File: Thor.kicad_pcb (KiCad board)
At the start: 4 copper layers, 300 x 200 mm, 41 parts, among them J1 Conn_02x32_Counter_Clockwise, J2 Conn_02x32_Counter_Clockwise, J3 Conn_01x01, J4 Conn_01x01, Q1 PHP79NQ08LT, Q2 PHP79NQ08LT, Q3 PHP79NQ08LT, Q4 PHP79NQ08LT, Q5 PHP79NQ08LT, Q6 PHP79NQ08LT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

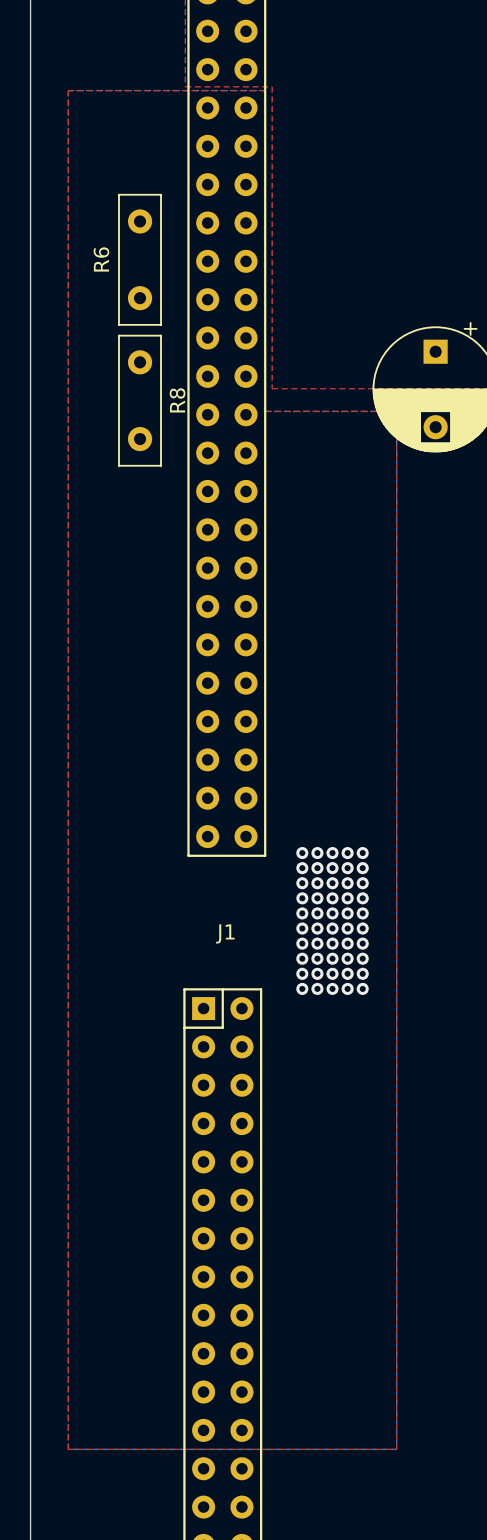
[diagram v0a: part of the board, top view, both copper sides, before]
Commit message: Revert "most recent version"
This reverts commit 98a59f1a5a33474df10b14d2ac29c781506322cc.
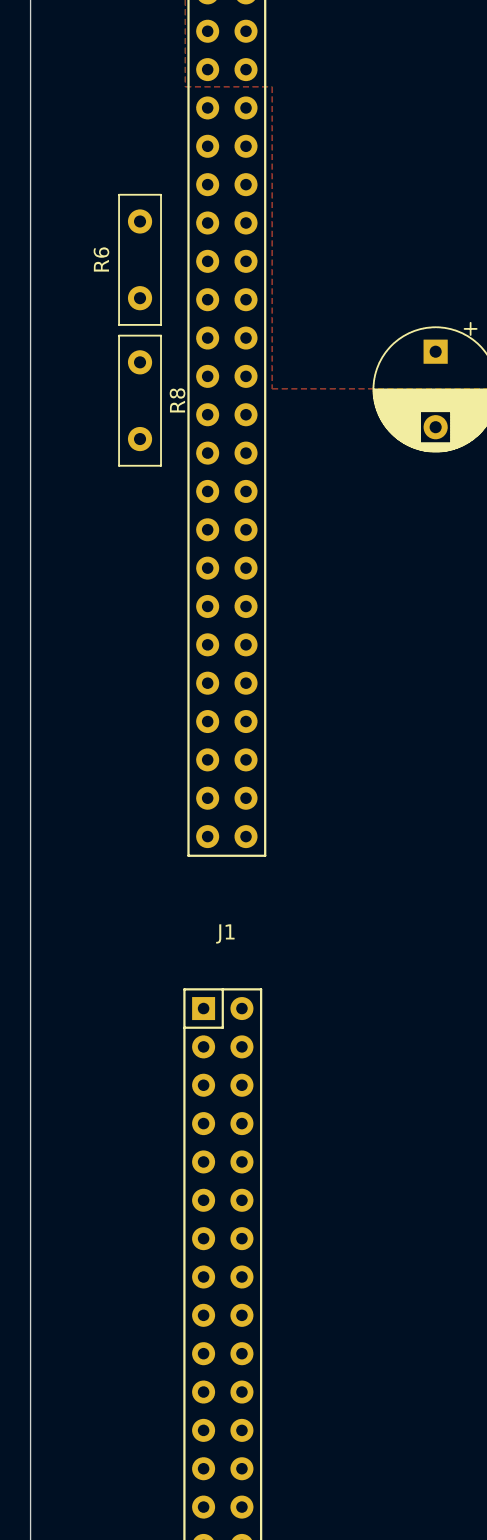
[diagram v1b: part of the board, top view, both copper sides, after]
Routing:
- net /12V_IN: vias 50 -> 0
- removed copper zone on B.Cu, net /12V_IN
- removed copper zone on F.Cu, net /12V_IN
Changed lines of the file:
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@@
     (thickness 1.6)
     (drawings 4)
-    (tracks 255)
+    (tracks 205)
     (zones 0)
     (modules 41)
@@
   (segment (start 157.9325 88.4) (end 158.48 88.9475) (width 0.25) (layer F.Cu) (net 42))
   (segment (start 156.4875 88.4) (end 157.9325 88.4) (width 0.25) (layer F.Cu) (net 42))
-  (via (at 28 100) (size 0.8) (drill 0.4) (layers F.Cu B.Cu) (net 44))
-  (via (at 29 100) (size 0.8) (drill 0.4) (layers F.Cu B.Cu) (net 44))
-  (via (at 30 100) (size 0.8) (drill 0.4) (layers F.Cu B.Cu) (net 44))
-  (via (at 31 100) (size 0.8) (drill 0.4) (layers F.Cu B.Cu) (net 44))
-  (via (at 32 100) (size 0.8) (drill 0.4) (layers F.Cu B.Cu) (net 44))
-  (via (at 28 101) (size 0.8) (drill 0.4) (layers F.Cu B.Cu) (net 44))
-  (via (at 29 101) (size 0.8) (drill 0.4) (layers F.Cu B.Cu) (net 44))
-  (via (at 30 101) (size 0.8) (drill 0.4) (layers F.Cu B.Cu) (net 44))
-  (via (at 31 101) (size 0.8) (drill 0.4) (layers F.Cu B.Cu) (net 44))
-  (via (at 32 101) (size 0.8) (drill 0.4) (layers F.Cu B.Cu) (net 44))
-  (via (at 28 102) (size 0.8) (drill 0.4) (layers F.Cu B.Cu) (net 44))
-  (via (at 29 102) (size 0.8) (drill 0.4) (layers F.Cu B.Cu) (net 44))
-  (via (at 30 102) (size 0.8) (drill 0.4) (layers F.Cu B.Cu) (net 44))
-  (via (at 31 102) (size 0.8) (drill 0.4) (layers F.Cu B.Cu) (net 44))
-  (via (at 32 102) (size 0.8) (drill 0.4) (layers F.Cu B.Cu) (net 44))
-  (via (at 28 103) (size 0.8) (drill 0.4) (layers F.Cu B.Cu) (net 44))
-  (via (at 29 103) (size 0.8) (drill 0.4) (layers F.Cu B.Cu) (net 44))
-  (via (at 30 103) (size 0.8) (drill 0.4) (layers F.Cu B.Cu) (net 44))
-  (via (at 31 103) (size 0.8) (drill 0.4) (layers F.Cu B.Cu) (net 44))
-  (via (at 32 103) (size 0.8) (drill 0.4) (layers F.Cu B.Cu) (net 44))
-  (via (at 28 104) (size 0.8) (drill 0.4) (layers F.Cu B.Cu) (net 44))
-  (via (at 29 104) (size 0.8) (drill 0.4) (layers F.Cu B.Cu) (net 44))
-  (via (at 30 104) (size 0.8) (drill 0.4) (layers F.Cu B.Cu) (net 44))
-  (via (at 31 104) (size 0.8) (drill 0.4) (layers F.Cu B.Cu) (net 44))
-  (via (at 32 104) (size 0.8) (drill 0.4) (layers F.Cu B.Cu) (net 44))
-  (via (at 28 105) (size 0.8) (drill 0.4) (layers F.Cu B.Cu) (net 44))
-  (via (at 29 105) (size 0.8) (drill 0.4) (layers F.Cu B.Cu) (net 44))
-  (via (at 30 105) (size 0.8) (drill 0.4) (layers F.Cu B.Cu) (net 44))
-  (via (at 31 105) (size 0.8) (drill 0.4) (layers F.Cu B.Cu) (net 44))
-  (via (at 32 105) (size 0.8) (drill 0.4) (layers F.Cu B.Cu) (net 44))
-  (via (at 28 106) (size 0.8) (drill 0.4) (layers F.Cu B.Cu) (net 44))
-  (via (at 29 106) (size 0.8) (drill 0.4) (layers F.Cu B.Cu) (net 44))
-  (via (at 30 106) (size 0.8) (drill 0.4) (layers F.Cu B.Cu) (net 44))
-  (via (at 31 106) (size 0.8) (drill 0.4) (layers F.Cu B.Cu) (net 44))
-  (via (at 32 106) (size 0.8) (drill 0.4) (layers F.Cu B.Cu) (net 44))
-  (via (at 28 107) (size 0.8) (drill 0.4) (layers F.Cu B.Cu) (net 44))
-  (via (at 29 107) (size 0.8) (drill 0.4) (layers F.Cu B.Cu) (net 44))
-  (via (at 30 107) (size 0.8) (drill 0.4) (layers F.Cu B.Cu) (net 44))
-  (via (at 31 107) (size 0.8) (drill 0.4) (layers F.Cu B.Cu) (net 44))
-  (via (at 32 107) (size 0.8) (drill 0.4) (layers F.Cu B.Cu) (net 44))
-  (via (at 28 108) (size 0.8) (drill 0.4) (layers F.Cu B.Cu) (net 44))
-  (via (at 29 108) (size 0.8) (drill 0.4) (layers F.Cu B.Cu) (net 44))
-  (via (at 30 108) (size 0.8) (drill 0.4) (layers F.Cu B.Cu) (net 44))
-  (via (at 31 108) (size 0.8) (drill 0.4) (layers F.Cu B.Cu) (net 44))
-  (via (at 32 108) (size 0.8) (drill 0.4) (layers F.Cu B.Cu) (net 44))
-  (via (at 28 109) (size 0.8) (drill 0.4) (layers F.Cu B.Cu) (net 44))
-  (via (at 29 109) (size 0.8) (drill 0.4) (layers F.Cu B.Cu) (net 44))
-  (via (at 30 109) (size 0.8) (drill 0.4) (layers F.Cu B.Cu) (net 44))
-  (via (at 31 109) (size 0.8) (drill 0.4) (layers F.Cu B.Cu) (net 44))
-  (via (at 32 109) (size 0.8) (drill 0.4) (layers F.Cu B.Cu) (net 44))
   (zone (net 32) (net_name /SW) (layer F.Cu) (hatch edge 0.508)
     (connect_pads yes (clearance 0.508))
@@
       )
     )
-  )
-  (zone (net 44) (net_name /12V_IN) (layer F.Cu) (hatch edge 0.508)
-    (connect_pads yes (clearance 0.508))
-    (min_thickness 0.254)
-    (fill yes (arc_segments 32) (thermal_gap 0.508) (thermal_bridge_width 5))
-    (polygon
-      (pts
-        (xy 25.5 49.5) (xy 12.5 49.5) (xy 12.5 139.5) (xy 34.25 139.5) (xy 34.25 70.75)
-        (xy 25.5 70.75)
-      )
-    )
-  )
-  (zone (net 44) (net_name /12V_IN) (layer B.Cu) (hatch edge 0.508)
-    (connect_pads yes (clearance 0.508))
-    (min_thickness 0.254)
-    (fill yes (arc_segments 32) (thermal_gap 0.508) (thermal_bridge_width 5))
-    (polygon
-      (pts
-        (xy 12.5 49.5) (xy 25.5 49.5) (xy 25.5 70.75) (xy 34.25 70.75) (xy 34.25 139.5)
-        (xy 12.5 139.5)
-      )
-    )

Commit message: most recent version
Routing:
- net /12V_IN: vias 0 -> 50
- added copper zone on B.Cu, net /12V_IN
- added copper zone on F.Cu, net /12V_IN
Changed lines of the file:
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@@
     (thickness 1.6)
     (drawings 4)
-    (tracks 205)
+    (tracks 255)
     (zones 0)
     (modules 41)
@@
   (segment (start 157.9325 88.4) (end 158.48 88.9475) (width 0.25) (layer F.Cu) (net 42))
   (segment (start 156.4875 88.4) (end 157.9325 88.4) (width 0.25) (layer F.Cu) (net 42))
+  (via (at 28 100) (size 0.8) (drill 0.4) (layers F.Cu B.Cu) (net 44))
+  (via (at 29 100) (size 0.8) (drill 0.4) (layers F.Cu B.Cu) (net 44))
+  (via (at 30 100) (size 0.8) (drill 0.4) (layers F.Cu B.Cu) (net 44))
+  (via (at 31 100) (size 0.8) (drill 0.4) (layers F.Cu B.Cu) (net 44))
+  (via (at 32 100) (size 0.8) (drill 0.4) (layers F.Cu B.Cu) (net 44))
+  (via (at 28 101) (size 0.8) (drill 0.4) (layers F.Cu B.Cu) (net 44))
+  (via (at 29 101) (size 0.8) (drill 0.4) (layers F.Cu B.Cu) (net 44))
+  (via (at 30 101) (size 0.8) (drill 0.4) (layers F.Cu B.Cu) (net 44))
+  (via (at 31 101) (size 0.8) (drill 0.4) (layers F.Cu B.Cu) (net 44))
+  (via (at 32 101) (size 0.8) (drill 0.4) (layers F.Cu B.Cu) (net 44))
+  (via (at 28 102) (size 0.8) (drill 0.4) (layers F.Cu B.Cu) (net 44))
+  (via (at 29 102) (size 0.8) (drill 0.4) (layers F.Cu B.Cu) (net 44))
+  (via (at 30 102) (size 0.8) (drill 0.4) (layers F.Cu B.Cu) (net 44))
+  (via (at 31 102) (size 0.8) (drill 0.4) (layers F.Cu B.Cu) (net 44))
+  (via (at 32 102) (size 0.8) (drill 0.4) (layers F.Cu B.Cu) (net 44))
+  (via (at 28 103) (size 0.8) (drill 0.4) (layers F.Cu B.Cu) (net 44))
+  (via (at 29 103) (size 0.8) (drill 0.4) (layers F.Cu B.Cu) (net 44))
+  (via (at 30 103) (size 0.8) (drill 0.4) (layers F.Cu B.Cu) (net 44))
+  (via (at 31 103) (size 0.8) (drill 0.4) (layers F.Cu B.Cu) (net 44))
+  (via (at 32 103) (size 0.8) (drill 0.4) (layers F.Cu B.Cu) (net 44))
+  (via (at 28 104) (size 0.8) (drill 0.4) (layers F.Cu B.Cu) (net 44))
+  (via (at 29 104) (size 0.8) (drill 0.4) (layers F.Cu B.Cu) (net 44))
+  (via (at 30 104) (size 0.8) (drill 0.4) (layers F.Cu B.Cu) (net 44))
+  (via (at 31 104) (size 0.8) (drill 0.4) (layers F.Cu B.Cu) (net 44))
+  (via (at 32 104) (size 0.8) (drill 0.4) (layers F.Cu B.Cu) (net 44))
+  (via (at 28 105) (size 0.8) (drill 0.4) (layers F.Cu B.Cu) (net 44))
+  (via (at 29 105) (size 0.8) (drill 0.4) (layers F.Cu B.Cu) (net 44))
+  (via (at 30 105) (size 0.8) (drill 0.4) (layers F.Cu B.Cu) (net 44))
+  (via (at 31 105) (size 0.8) (drill 0.4) (layers F.Cu B.Cu) (net 44))
+  (via (at 32 105) (size 0.8) (drill 0.4) (layers F.Cu B.Cu) (net 44))
+  (via (at 28 106) (size 0.8) (drill 0.4) (layers F.Cu B.Cu) (net 44))
+  (via (at 29 106) (size 0.8) (drill 0.4) (layers F.Cu B.Cu) (net 44))
+  (via (at 30 106) (size 0.8) (drill 0.4) (layers F.Cu B.Cu) (net 44))
+  (via (at 31 106) (size 0.8) (drill 0.4) (layers F.Cu B.Cu) (net 44))
+  (via (at 32 106) (size 0.8) (drill 0.4) (layers F.Cu B.Cu) (net 44))
+  (via (at 28 107) (size 0.8) (drill 0.4) (layers F.Cu B.Cu) (net 44))
+  (via (at 29 107) (size 0.8) (drill 0.4) (layers F.Cu B.Cu) (net 44))
+  (via (at 30 107) (size 0.8) (drill 0.4) (layers F.Cu B.Cu) (net 44))
+  (via (at 31 107) (size 0.8) (drill 0.4) (layers F.Cu B.Cu) (net 44))
+  (via (at 32 107) (size 0.8) (drill 0.4) (layers F.Cu B.Cu) (net 44))
+  (via (at 28 108) (size 0.8) (drill 0.4) (layers F.Cu B.Cu) (net 44))
+  (via (at 29 108) (size 0.8) (drill 0.4) (layers F.Cu B.Cu) (net 44))
+  (via (at 30 108) (size 0.8) (drill 0.4) (layers F.Cu B.Cu) (net 44))
+  (via (at 31 108) (size 0.8) (drill 0.4) (layers F.Cu B.Cu) (net 44))
+  (via (at 32 108) (size 0.8) (drill 0.4) (layers F.Cu B.Cu) (net 44))
+  (via (at 28 109) (size 0.8) (drill 0.4) (layers F.Cu B.Cu) (net 44))
+  (via (at 29 109) (size 0.8) (drill 0.4) (layers F.Cu B.Cu) (net 44))
+  (via (at 30 109) (size 0.8) (drill 0.4) (layers F.Cu B.Cu) (net 44))
+  (via (at 31 109) (size 0.8) (drill 0.4) (layers F.Cu B.Cu) (net 44))
+  (via (at 32 109) (size 0.8) (drill 0.4) (layers F.Cu B.Cu) (net 44))
   (zone (net 32) (net_name /SW) (layer F.Cu) (hatch edge 0.508)
     (connect_pads yes (clearance 0.508))
@@
       )
     )
+  )
+  (zone (net 44) (net_name /12V_IN) (layer F.Cu) (hatch edge 0.508)
+    (connect_pads yes (clearance 0.508))
+    (min_thickness 0.254)
+    (fill yes (arc_segments 32) (thermal_gap 0.508) (thermal_bridge_width 5))
+    (polygon
+      (pts
+        (xy 25.5 49.5) (xy 12.5 49.5) (xy 12.5 139.5) (xy 34.25 139.5) (xy 34.25 70.75)
+        (xy 25.5 70.75)
+      )
+    )
+  )
+  (zone (net 44) (net_name /12V_IN) (layer B.Cu) (hatch edge 0.508)
+    (connect_pads yes (clearance 0.508))
+    (min_thickness 0.254)
+    (fill yes (arc_segments 32) (thermal_gap 0.508) (thermal_bridge_width 5))
+    (polygon
+      (pts
+        (xy 12.5 49.5) (xy 25.5 49.5) (xy 25.5 70.75) (xy 34.25 70.75) (xy 34.25 139.5)
+        (xy 12.5 139.5)
+      )
+    )
